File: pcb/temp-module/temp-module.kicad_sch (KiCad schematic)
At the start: 12 parts, among them J1 Connector_male, J2 Screw_Terminal_01x02, U1 MCP6002-xSN

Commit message: update pcb
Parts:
- J2: footprint TerminalBlock:TerminalBlock_bornier-2_P5.08mm -> TerminalBlock_Phoenix:TerminalBlock_Phoenix_MKDS-1,5-2-5.08_1x02_P5.08mm_Horizontal
- renumbered R6 to R1, R1 to R3, R5 to R4, R4 to R5, R3 to R6
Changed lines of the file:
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@@
   (symbol (lib_id "Device:R") (at 67.31 39.37 90) (unit 1)
     (in_bom yes) (on_board yes)
-    (property "Reference" "R3" (id 0) (at 67.31 36.83 90))
+    (property "Reference" "R6" (id 0) (at 67.31 36.83 90))
     (property "Value" "5.1K" (id 1) (at 67.31 40.64 90)
       (effects (font (size 1.27 1.27)) (justify bottom))
@@
       (effects (font (size 1.27 1.27)) (justify left) hide)
     )
-    (property "Footprint" "TerminalBlock:TerminalBlock_bornier-2_P5.08mm" (id 2) (at 96.52 19.05 0)
+    (property "Footprint" "TerminalBlock_Phoenix:TerminalBlock_Phoenix_MKDS-1,5-2-5.08_1x02_P5.08mm_Horizontal" (id 2) (at 96.52 19.05 0)
       (effects (font (size 1.27 1.27)) hide)
     )
@@
   (symbol (lib_id "Device:R") (at 87.63 53.34 0) (unit 1)
     (in_bom yes) (on_board yes)
-    (property "Reference" "R6" (id 0) (at 85.09 54.61 90)
+    (property "Reference" "R1" (id 0) (at 85.09 54.61 90)
       (effects (font (size 1.27 1.27)) (justify left))
     )
@@
   (symbol (lib_id "Device:R") (at 80.01 39.37 90) (unit 1)
     (in_bom yes) (on_board yes)
-    (property "Reference" "R4" (id 0) (at 80.01 36.83 90))
+    (property "Reference" "R5" (id 0) (at 80.01 36.83 90))
     (property "Value" "330R" (id 1) (at 80.01 40.64 90)
       (effects (font (size 1.27 1.27)) (justify bottom))
@@
   (symbol (lib_id "Device:R") (at 67.31 46.99 270) (unit 1)
     (in_bom yes) (on_board yes)
-    (property "Reference" "R1" (id 0) (at 67.31 44.45 90))
+    (property "Reference" "R3" (id 0) (at 67.31 44.45 90))
     (property "Value" "1.3K" (id 1) (at 67.31 49.53 90))
     (property "Footprint" "Resistor_SMD:R_0805_2012Metric" (id 2) (at 67.31 45.212 90)
@@
   (symbol (lib_id "Device:R") (at 87.63 33.02 0) (unit 1)
     (in_bom yes) (on_board yes)
-    (property "Reference" "R5" (id 0) (at 85.09 33.02 90))
+    (property "Reference" "R4" (id 0) (at 85.09 33.02 90))
     (property "Value" "5.1K" (id 1) (at 90.17 33.02 90))
     (property "Footprint" "Resistor_SMD:R_0805_2012Metric" (id 2) (at 85.852 33.02 90)
@@
     )
     (path "/173336f1-9601-4b41-8945-5c6f79af3be1"
-      (reference "J2") (unit 1) (value "Screw_Terminal_01x02") (footprint "TerminalBlock:TerminalBlock_bornier-2_P5.08mm")
-    )
-    (path "/a0c966ca-26d6-4690-917b-5f4512eab87e"
-      (reference "R1") (unit 1) (value "1.3K") (footprint "Resistor_SMD:R_0805_2012Metric")
+      (reference "J2") (unit 1) (value "Screw_Terminal_01x02") (footprint "TerminalBlock_Phoenix:TerminalBlock_Phoenix_MKDS-1,5-2-5.08_1x02_P5.08mm_Horizontal")
+    )
+    (path "/3362f1dc-45f1-4f3c-966f-894e97681dff"
+      (reference "R1") (unit 1) (value "110K") (footprint "Resistor_SMD:R_0805_2012Metric")
     )
     (path "/9ccb8105-fc77-4b12-80e3-98af7225c931"
       (reference "R2") (unit 1) (value "10K") (footprint "Resistor_SMD:R_0805_2012Metric")
     )
+    (path "/a0c966ca-26d6-4690-917b-5f4512eab87e"
+      (reference "R3") (unit 1) (value "1.3K") (footprint "Resistor_SMD:R_0805_2012Metric")
+    )
+    (path "/c4be59be-7931-4777-93de-18f231b213e1"
+      (reference "R4") (unit 1) (value "5.1K") (footprint "Resistor_SMD:R_0805_2012Metric")
+    )
+    (path "/6ffda4ba-a353-468a-8e5c-66b431ec911c"
+      (reference "R5") (unit 1) (value "330R") (footprint "Resistor_SMD:R_0805_2012Metric")
+    )
     (path "/0186bdee-143a-4768-8c13-d163f780ad88"
-      (reference "R3") (unit 1) (value "5.1K") (footprint "Resistor_SMD:R_0805_2012Metric")
-    )
-    (path "/6ffda4ba-a353-468a-8e5c-66b431ec911c"
-      (reference "R4") (unit 1) (value "330R") (footprint "Resistor_SMD:R_0805_2012Metric")
-    )
-    (path "/c4be59be-7931-4777-93de-18f231b213e1"
-      (reference "R5") (unit 1) (value "5.1K") (footprint "Resistor_SMD:R_0805_2012Metric")
-    )
-    (path "/3362f1dc-45f1-4f3c-966f-894e97681dff"
-      (reference "R6") (unit 1) (value "110K") (footprint "Resistor_SMD:R_0805_2012Metric")
+      (reference "R6") (unit 1) (value "5.1K") (footprint "Resistor_SMD:R_0805_2012Metric")
     )
     (path "/59d51535-b0f8-4434-b2a3-1d9db5e1ebff"

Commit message: temp-calibrate
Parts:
- removed J2: Screw_Terminal_01x02, TerminalBlock_Phoenix:TerminalBlock_Phoenix_MKDS-1,5-2-5.08_1x02_P5.08mm_Horizontal, symbol Connector:Screw_Terminal_01x02
- removed R1: 110K, Resistor_SMD:R_0805_2012Metric, symbol Device:R
- removed R2: 10K, Resistor_SMD:R_0805_2012Metric, symbol Device:R
- removed R4, R6: 5.1K, Resistor_SMD:R_0805_2012Metric, symbol Device:R
- removed U1: MCP6002-xSN, Package_DIP:DIP-8_W7.62mm, symbol Amplifier_Operational:MCP6002-xSN
- added C4: 100nF, Capacitor_SMD:C_1206_3216Metric, symbol Device:C
- added J2: Screw_Terminal_01x03, Connector_Wago:Wago_734-163_1x03_P3.50mm_Horizontal, symbol Connector:Screw_Terminal_01x03
- added R1_1, R2_2: 1.3k, Resistor_SMD:R_0805_2012Metric, symbol Device:R
- added R1_2, R4_1: 2k, Resistor_SMD:R_0805_2012Metric, symbol Device:R
- added R1_3: 10k, Resistor_SMD:R_0805_2012Metric, symbol Device:R
- added R2_1: 330, Resistor_SMD:R_0805_2012Metric, symbol Device:R
- added R2_3: 110k, Resistor_SMD:R_0805_2012Metric, symbol Device:R
- added R4_2: 2.4k, Resistor_SMD:R_0805_2012Metric, symbol Device:R
- added R4_3: 20k, Resistor_SMD:R_0805_2012Metric, symbol Device:R
- added U1: MCP6002-xP, Package_DIP:DIP-8_W7.62mm, symbol Amplifier_Operational:MCP6002-xP
- C1, C2: value 0.1uF -> 100nF
- R3: value 1.3K -> 20k
- R5: value 330R -> 1k
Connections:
- net U5_OP+ is gone; now on net +5V: R5.2
- net +5V: now also R3.1, U1.8 (V+)
- net GND: now also C4.1, J2.3 (Pin_3), R4_1.1, U1.4 (V-); no longer R3.2
- net S1: now also J2.1 (Pin_1), U1.5 (+); no longer R3.1
- net SREG: now also C4.2, R2_3.2, U1.7
- net R4-5 renamed S2
- net S2: now also J2.2 (Pin_2)
- new net R_1_1_2: R1_1.2, R1_2.1
- new net R_1_2_3: R1_2.2, R1_3.1
- new net R_2_1_2: R2_1.2, R2_2.1
- new net R_2_2_3: R2_2.2, R2_3.1
- new net R_4_1_2: R4_1.2, R4_2.1
- new net R_4_2_3: R4_2.2, R4_3.1
- new net fb: R1_3.2, R2_1.1, U1.6 (-)
- new net vk_buf: R1_1.1, U1.1, U1.2 (-)
- new net vk_in: R3.2, R4_3.2, U1.3 (+)
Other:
- note added: "ATMega"
- note added: "Filter/ Buffer Capacitors"
- note added: "Front Terminal"
- note added: "Power Input"
- moved on the sheet: C1, C2, C3, J1A, J1B

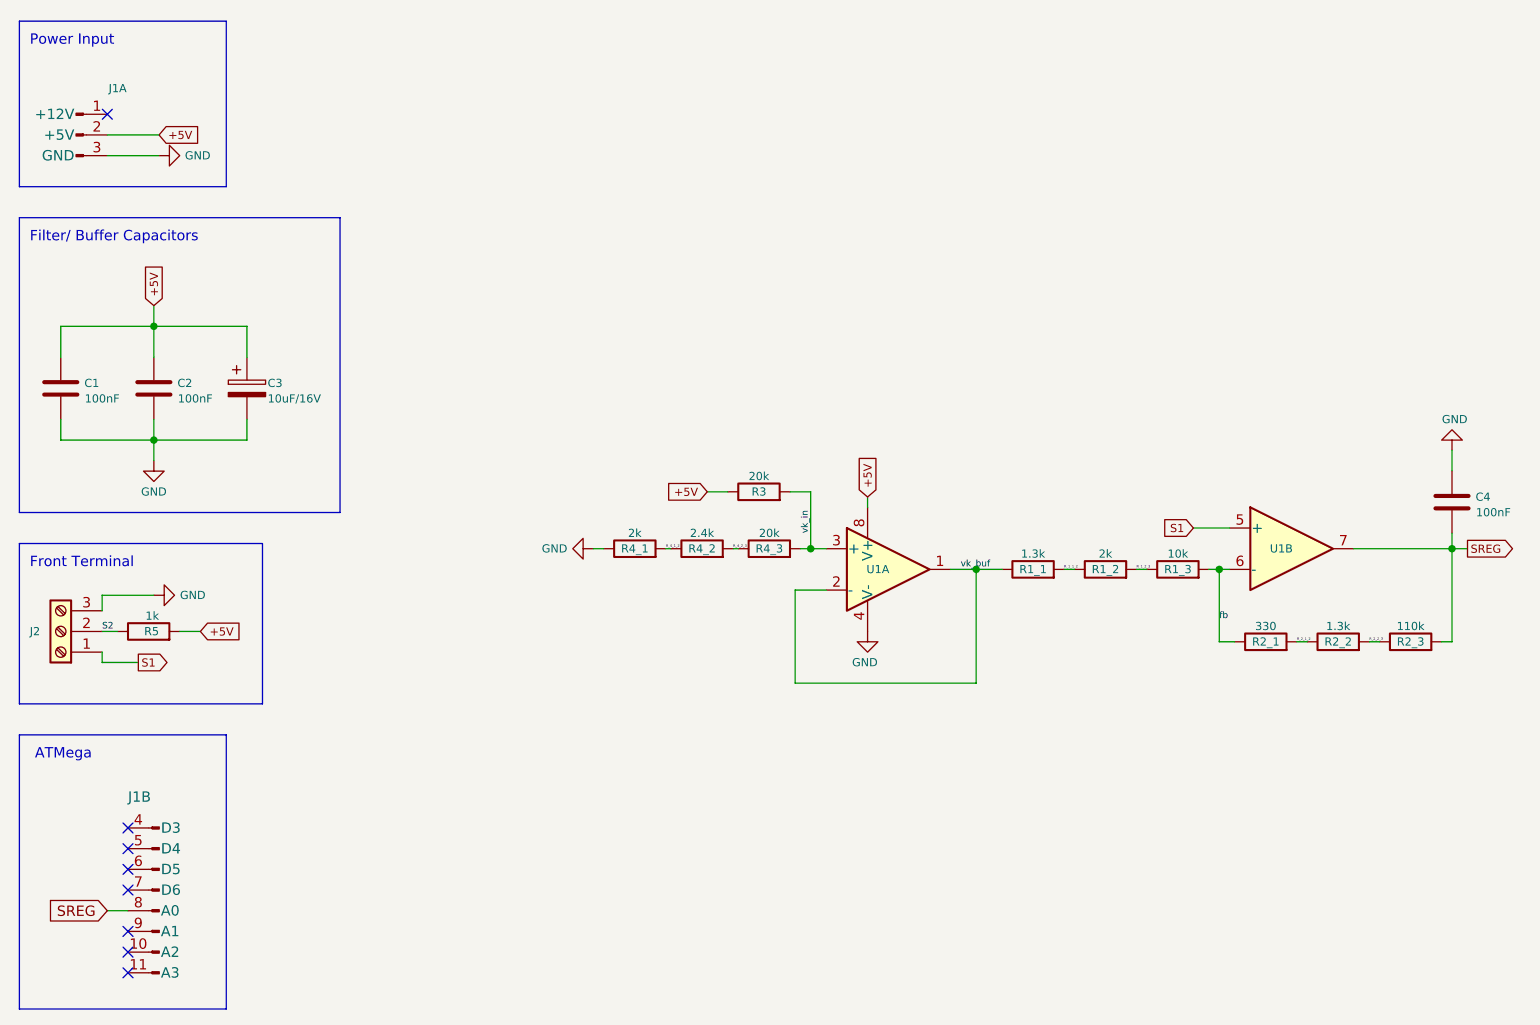
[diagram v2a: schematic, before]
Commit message: new temp module
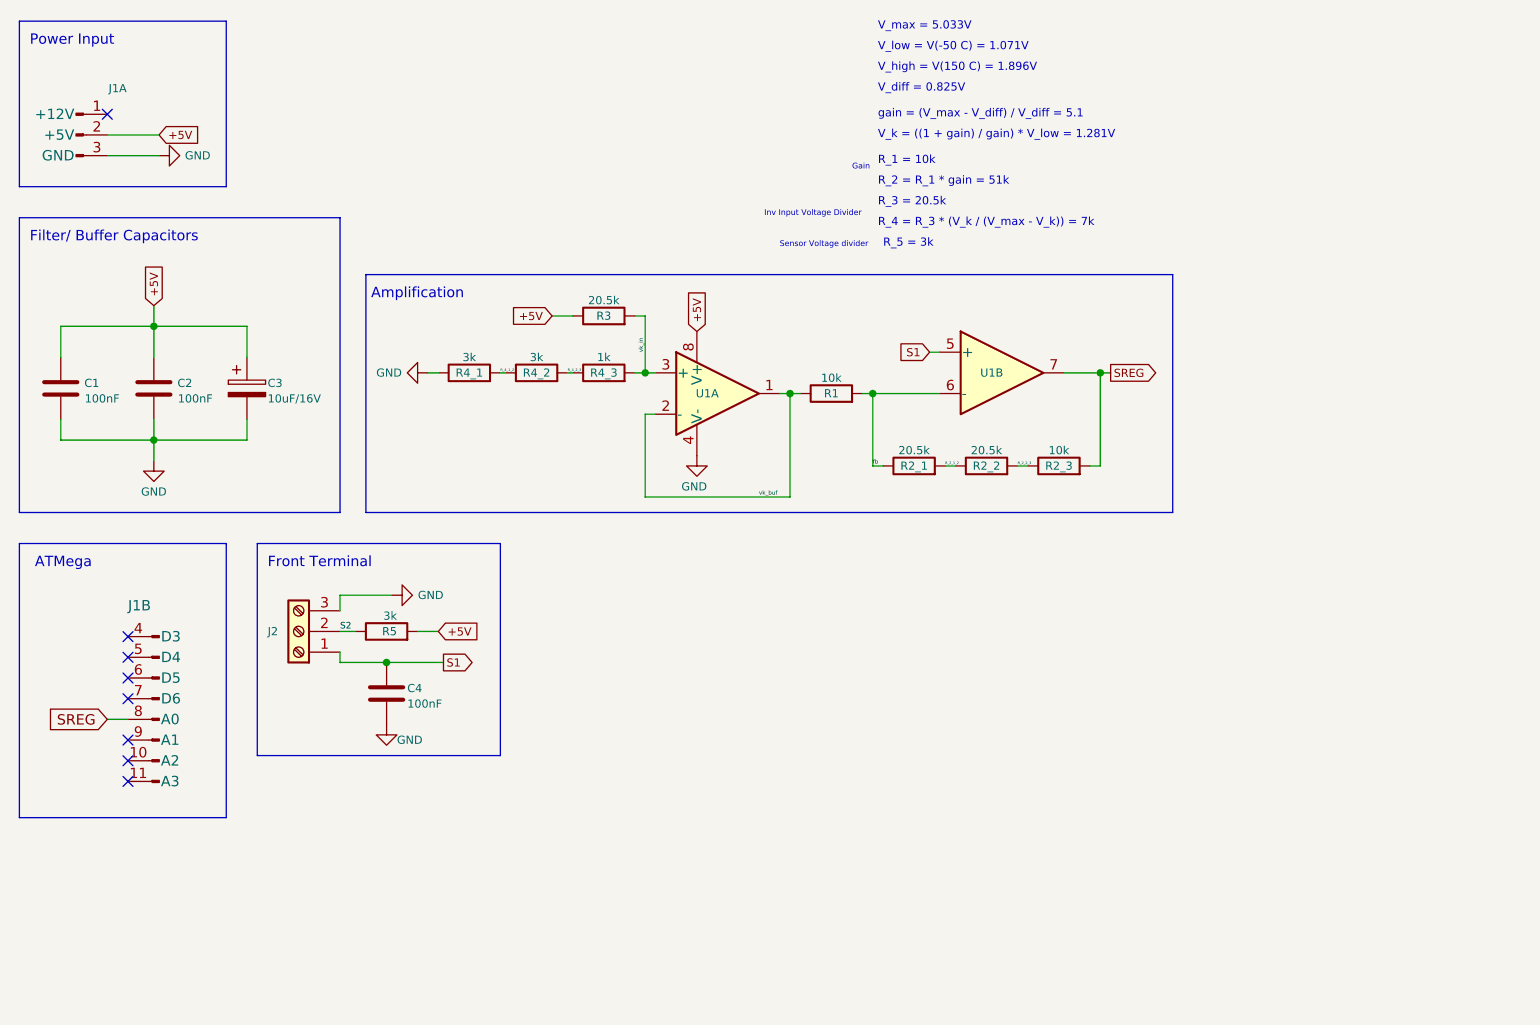
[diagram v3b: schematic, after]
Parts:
- removed R1_2: 2k, Resistor_SMD:R_0805_2012Metric, symbol Device:R
- removed R1_3: 10k, Resistor_SMD:R_0805_2012Metric, symbol Device:R
- R1: renamed from R1_1; value 1.3k -> 10k
- R2_1: value 330 -> 20.5k
- R2_2: value 1.3k -> 20.5k
- R2_3: value 110k -> 10k
- R3: value 20k -> 20.5k
- R4_1: value 2k -> 3k
- R4_2: value 2.4k -> 3k
- R4_3: value 20k -> 1k
- R5: value 1k -> 3k
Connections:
- net R_1_1_2 is gone; now on net fb: R1.2
- net GND: now also C4.2; no longer C4.1
- net S1: now also C4.1
- net SREG: no longer C4.2
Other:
- note added: "Amplification"
- note added: "Gain"
- note added: "Inv Input Voltage Divider"
- note added: "R_1 = 10k"
- note added: "R_2 = R_1 * gain = 51k"
- note added: "R_3 = 20.5k"
- note added: "R_4 = R_3 * (V_k / (V_max - V_k)) = 7k"
- note added: "R_5 = 3k"
- note added: "Sensor Voltage divider"
- note added: "V_diff = 0.825V"
- note added: "V_high = V(150 C) = 1.896V"
- note added: "V_k = ((1 + gain) / gain) * V_low = 1.281V"
- note added: "V_low = V(-50 C) = 1.071V"
- note added: "V_max = 5.033V"
- note added: "gain = (V_max - V_diff) / V_diff = 5.1"
- moved on the sheet: J1B, J2, R1, R2_1, R2_2, R2_3, R3, R4_1, R4_2, R4_3, R5, U1A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

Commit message: pcb update
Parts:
- removed C2: 100nF, Capacitor_SMD:C_1206_3216Metric, symbol Device:C
- removed J1: Connector_male, CAN_ATmega:Connector_male, symbol CAN-ATmega:Connector_male
- added J1: Connector_male_4x8, CAN_ATmega:Connector_male_4x8, symbol CAN-ATmega:Connector_male_4x8
- renumbered C3 to C1, C1 to C2
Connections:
- net GND: now also J1.4 (GND)
- net SREG: now also J1.9 (A0)
- net +5V renamed AVCC
- net AVCC: now also J1.3 (AVCC)
- no-connect marks 8 -> 9
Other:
- moved on the sheet: C1, C2
